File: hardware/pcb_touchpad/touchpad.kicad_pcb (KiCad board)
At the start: 2 copper layers, 41.3 x 30.3 mm, 24 parts, among them U1 IQS9151

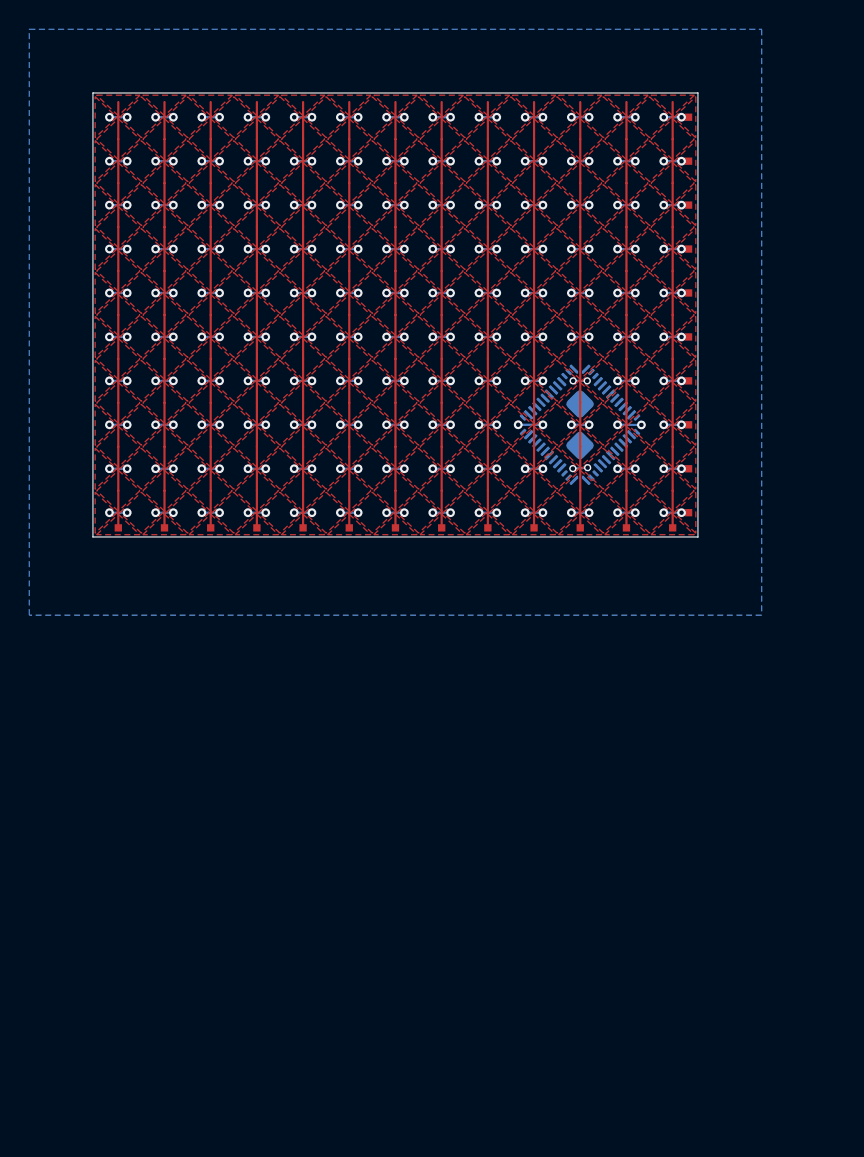
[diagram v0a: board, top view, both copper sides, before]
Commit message: touchpad: regenerated touchpad, made IQS7211E symbol
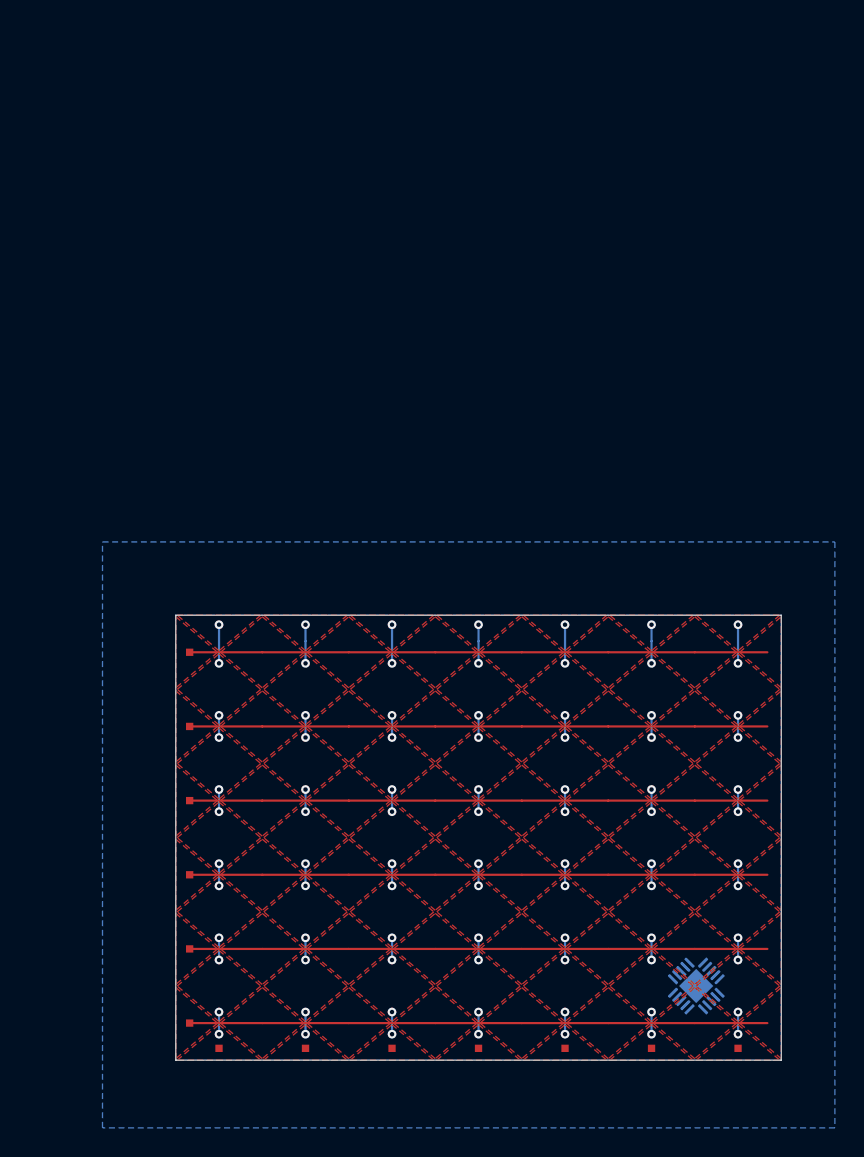
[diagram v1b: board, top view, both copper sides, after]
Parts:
- removed COL10, COL8, COL9, ROW10, ROW11, ROW12, ROW13, ROW7, ROW8, ROW9: TESTPOINTPAD_0_5MM, PAD_0_5MM
- U1: value IQS9151 -> IQS7211E; footprint Package_DFN_QFN:VQFN-52-1EP_6x6mm_P0.4mm_EP4.7x4.7mm -> Package_DFN_QFN:QFN-20-1EP_3x3mm_P0.4mm_EP1.65x1.65mm
- moved COL7 54.7 mm to (186.9, 134.6), turned to 0 degrees
- moved COL6 51.6 mm to (181.0, 134.6), turned to 0 degrees
- moved COL5 49.3 mm to (175.1, 134.6), turned to 0 degrees
- moved COL1 48.6 mm to (151.5, 134.6), turned to 0 degrees
- moved COL4 47.8 mm to (169.2, 134.6), turned to 0 degrees
- moved COL2 47.4 mm to (157.4, 134.6), turned to 0 degrees
- moved ROW1 47.2 mm to (149.5, 132.9), turned to 0 degrees
- moved COL3 47.1 mm to (163.3, 134.6), turned to 0 degrees
- moved ROW2 41.4 mm to (149.5, 127.8), turned to 0 degrees
- moved U1 39.1 mm to (184.0, 130.3), turned to 135 degrees
- moved ROW3 35.7 mm to (149.5, 122.7), turned to 0 degrees
- moved ROW4 30.0 mm to (149.5, 117.7), turned to 0 degrees
- moved ROW5 24.5 mm to (149.5, 112.6), turned to 0 degrees
- moved ROW6 19.2 mm to (149.5, 107.5), turned to 0 degrees
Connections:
- U1 pad 10: unconnected-(U1-NC-Pad10) -> /COL2
- U1 pad 11: /COL8 -> /COL1
- U1 pad 12: unconnected-(U1-NC-Pad12) -> /ROW6
- U1 pad 13: unconnected-(U1-NC-Pad13) -> /ROW5
- U1 pad 14: /COL7 -> /ROW4
- U1 pad 15: unconnected-(U1-NC-Pad15) -> /ROW3
- U1 pad 16: /COL6 -> /ROW2
- U1 pad 17: unconnected-(U1-NC-Pad17) -> /ROW1
- U1 pad 19: /COL5 -> unconnected-(U1-SDA-Pad19)
- U1 pad 21: /COL4 -> GND
- U1 pad 5: unconnected-(U1-VREG-Pad5) -> /COL7
- U1 pad 6: /COL10 -> /COL6
- U1 pad 7: unconnected-(U1-NC-Pad7) -> /COL5
- U1 pad 8: /COL9 -> /COL4
- U1 pad 9: unconnected-(U1-NC-Pad9) -> /COL3
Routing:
- net (no net): track 0.00 -> 71.4 mm, vias 0 -> 84
- net /ROW12: track 29.1 -> 0.00 mm
- net /ROW10: track 29.1 -> 0.00 mm
- net /ROW9: track 29.1 -> 0.00 mm
- net /ROW11: track 29.1 -> 0.00 mm
- net /ROW: track 29.1 -> 0.00 mm
- net /ROW8: track 29.1 -> 0.00 mm
- net /ROW13: track 29.1 -> 0.00 mm
- net /COL3: track 16.6 -> 0.00 mm, vias 26 -> 0
- net /COL9: track 15.8 -> 0.00 mm, vias 26 -> 0
- net /COL8: track 15.8 -> 0.00 mm, vias 26 -> 0
- net /COL7: track 15.8 -> 0.00 mm, vias 26 -> 0
- net /COL6: track 15.8 -> 0.00 mm, vias 26 -> 0
- net /COL5: track 15.8 -> 0.00 mm, vias 26 -> 0
- net /COL10: track 15.8 -> 0.00 mm, vias 26 -> 0
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- removed copper zone on F.Cu, net /COL10
- removed copper zone on F.Cu, net /COL8
- removed copper zone on F.Cu, net /COL9
- removed copper zone on F.Cu, net /ROW
- removed copper zone on F.Cu, net /ROW10
- removed copper zone on F.Cu, net /ROW11
- removed copper zone on F.Cu, net /ROW12
- removed copper zone on F.Cu, net /ROW13
- removed copper zone on F.Cu, net /ROW8
- removed copper zone on F.Cu, net /ROW9
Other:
- board size 41.3 x 30.3 mm -> 41.3 x 30.4 mm

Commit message: touchpad: changed nets for col vias, removed mask opening for test pads
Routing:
- net (no net): track 71.4 -> 0.00 mm, vias 84 -> 0
- net /COL7: track 0.00 -> 10.2 mm, vias 0 -> 12
- net /COL6: track 0.00 -> 10.2 mm, vias 0 -> 12
- net /COL5: track 0.00 -> 10.2 mm, vias 0 -> 12
- net /COL4: track 0.00 -> 10.2 mm, vias 0 -> 12
- net /COL3: track 0.00 -> 10.2 mm, vias 0 -> 12
- net /COL2: track 0.00 -> 10.2 mm, vias 0 -> 12
- net /COL1: track 0.00 -> 10.2 mm, vias 0 -> 12

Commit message: touchpad: moved stuff around
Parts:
- moved U1 23.7 mm to (160.3, 130.3)
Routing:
- net /COL7: track 10.2 -> 9.07 mm
- net /COL6: track 10.2 -> 9.07 mm
- net /COL5: track 10.2 -> 9.07 mm
- net /COL4: track 10.2 -> 9.07 mm
- net /COL3: track 10.2 -> 9.07 mm
- net /COL2: track 10.2 -> 9.07 mm
- net /COL1: track 10.2 -> 9.07 mm
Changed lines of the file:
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@@
 		(filling no)
 		(aux_axis_origin 148.5011 105.0036)
-		(grid_origin 148.5011 105.0036)
+		(grid_origin 154.4061 130.3186)
 		(pcbplotparams
 			(layerselection 0x00000000_00000000_55555555_5755f5ff)
@@
 	(footprint "Package_DFN_QFN:QFN-20-1EP_3x3mm_P0.4mm_EP1.65x1.65mm"
 		(layer "B.Cu")
-		(at 184.037545 130.3203 135)
+		(at 160.310065 130.3136 135)
 		(descr "QFN, 20 Pin (https://www.analog.com/media/en/technical-documentation/data-sheets/3553fc.pdf#page=34)")
 		(tags "QFN NoLead")
@@
 	)
 	(via
-		(at 151.453946 105.653612)
+		(at 151.453946 106.77924)
 		(size 0.6)
 		(drill 0.3)
@@
 	)
 	(segment
-		(start 151.453946 105.653612)
-		(end 151.453946 106.77924)
-		(width 0.15)
-		(layer "B.Cu")
-		(net "/COL1")
-	)
-	(segment
 		(start 151.45395 108.29134)
 		(end 151.45395 106.77924)
@@
 	)
 	(via
-		(at 169.1711 105.653612)
+		(at 169.1711 106.77924)
 		(size 0.6)
 		(drill 0.3)
@@
 	)
 	(segment
-		(start 169.1711 105.653612)
-		(end 169.1711 106.77924)
-		(width 0.15)
-		(layer "B.Cu")
-		(net "/COL4")
-	)
-	(segment
 		(start 169.1711 108.29134)
 		(end 169.1711 106.77924)
@@
 	)
 	(via
-		(at 175.0768 105.653612)
+		(at 175.0768 106.77924)
 		(size 0.6)
 		(drill 0.3)
@@
 	)
 	(segment
-		(start 175.0768 105.653612)
-		(end 175.0768 106.77924)
-		(width 0.15)
-		(layer "B.Cu")
-		(net "/COL5")
-	)
-	(segment
 		(start 175.0768 133.608)
 		(end 175.0768 132.0959)
@@
 	)
 	(via
-		(at 157.359633 105.653612)
+		(at 157.359633 106.77924)
 		(size 0.6)
 		(drill 0.3)
@@
 	)
 	(segment
-		(start 157.359633 105.653612)
-		(end 157.359633 106.77924)
-		(width 0.15)
-		(layer "B.Cu")
-		(net "/COL2")
-	)
-	(segment
 		(start 149.450034 122.725266)
 		(end 154.4068 122.725275)
@@
 	)
 	(via
-		(at 163.2654 105.653612)
+		(at 163.2654 106.77924)
 		(size 0.6)
 		(drill 0.3)
@@
 	)
 	(segment
-		(start 163.2654 105.653612)
-		(end 163.2654 106.77924)
-		(width 0.15)
-		(layer "B.Cu")
-		(net "/COL3")
-	)
-	(segment
 		(start 163.2654 113.35468)
 		(end 163.2654 111.84257)
@@
 	)
 	(via
-		(at 186.8882 105.653612)
+		(at 186.8882 106.77924)
 		(size 0.6)
 		(drill 0.3)
@@
 	)
 	(segment
-		(start 186.8882 105.653612)
-		(end 186.8882 106.77924)
-		(width 0.15)
-		(layer "B.Cu")
-		(net "/COL7")
-	)
-	(segment
 		(start 186.8882 128.5447)
 		(end 186.8882 127.0326)
@@
 	)
 	(via
-		(at 180.9825 105.653612)
+		(at 180.9825 106.77924)
 		(size 0.6)
 		(drill 0.3)
@@
 	)
 	(segment
-		(start 180.9825 105.653612)
-		(end 180.9825 106.77924)
-		(width 0.15)
-		(layer "B.Cu")
-		(net "/COL6")
-	)
-	(segment
 		(start 180.9825 133.608)
 		(end 180.9825 132.0959)
@@
 		(name "GND Fill")
 		(hatch edge 0.5)
-		(connect_pads
+		(connect_pads yes
 			(clearance 0.15)
 		)

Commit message: added conn to trackpad pcb, updated mockup, placed conn
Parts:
- added J1: 503480-0540, 5034800540:503480-0540, B.Cu at (151.5, 113.1)
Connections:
- U1 pad 18: unconnected-(U1-SCL-Pad18) -> Net-(U1-SCL)
- U1 pad 19: unconnected-(U1-SDA-Pad19) -> Net-(U1-SDA)
- U1 pad 20: unconnected-(U1-RDY/MCLR-Pad20) -> Net-(U1-RDY/MCLR)

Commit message: small stuff
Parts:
- added C1: 1u, Capacitor_SMD:C_0402_1005Metric, B.Cu at (155.9, 132.2)
- added C2: 1u, Capacitor_SMD:C_0402_1005Metric, B.Cu at (157.5, 131.3)
- added C3: 1u, Capacitor_SMD:C_0402_1005Metric, B.Cu at (157.7, 130.4)
- moved U1 5.99 mm to (154.4, 129.3)
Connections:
- J1 pad 4: +3V3 -> Net-(U1-RDY/MCLR)
- J1 pad 5: Net-(U1-RDY/MCLR) -> +3V3
- U1 pad 1: unconnected-(U1-VDD-Pad1) -> +3V3
- U1 pad 2: unconnected-(U1-VREGD-Pad2) -> Net-(U1-VREGD)
- U1 pad 4: unconnected-(U1-VREGA-Pad4) -> Net-(U1-VREGA)
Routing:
- net /ROW1: track 39.4 -> 81.6 mm, vias 0 -> 1
- net /COL7: track 9.07 -> 45.7 mm
- net /COL6: track 9.07 -> 40.4 mm
- net /COL2: track 9.07 -> 40.2 mm
- net /COL5: track 9.07 -> 35.4 mm
- net /ROW6: track 39.4 -> 63.9 mm, vias 0 -> 1
- net +3V3: track 0.00 -> 21.8 mm
- net Net-(U1-SCL): track 0.00 -> 21.5 mm
- net Net-(U1-SDA): track 0.00 -> 21.1 mm
- net /COL4: track 9.07 -> 30.1 mm
- net Net-(U1-RDY/MCLR): track 0.00 -> 20.8 mm
- net /ROW5: track 39.4 -> 57.5 mm, vias 0 -> 1
- net /COL3: track 9.07 -> 24.3 mm
- net /ROW4: track 39.4 -> 51.3 mm, vias 0 -> 1
- net /ROW3: track 39.4 -> 42.9 mm, vias 0 -> 1
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
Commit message: first touchpad draft
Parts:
- J1: footprint 5034800540:503480-0540 -> 503480-0540:503480-0540
- moved C3 5.32 mm to (154.3, 126.3), turned to 45 degrees
- moved C2 4.88 mm to (156.1, 126.7), turned to 45 degrees
- moved C1 3.58 mm to (157.8, 129.2), turned to 0 degrees
- turned U1 to -135 degrees
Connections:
- net Net-(U1-RDY/MCLR) renamed /RDY/MCLR
- net Net-(U1-SCL) renamed /SCL
- net Net-(U1-SDA) renamed /SDA
- net Net-(U1-VREGA) renamed /VREGA
- net Net-(U1-VREGD) renamed /VREGD
- J1 pad MP_1: (no net) -> GND
- J1 pad MP_2: (no net) -> GND
- U1 pad 12: /ROW6 -> /ROW1
- U1 pad 13: /ROW5 -> /ROW2
- U1 pad 14: /ROW4 -> /ROW3
- U1 pad 15: /ROW3 -> /ROW4
- U1 pad 16: /ROW2 -> /ROW5
- U1 pad 17: /ROW1 -> /ROW6
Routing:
- net /ROW1: track 81.6 -> 44.2 mm
- net /COL2: track 40.2 -> 11.8 mm
- net +3V3: track 21.8 -> 14.1 mm
- net /RDY/MCLR: track 20.8 -> 13.9 mm
- net /SDA: track 21.1 -> 14.3 mm
- net /SCL: track 21.5 -> 14.9 mm
- net /COL4: track 30.1 -> 23.6 mm
- net /COL3: track 24.3 -> 17.8 mm
- net /COL5: track 35.4 -> 29.3 mm
- net /ROW3: track 42.9 -> 48.8 mm
- net /COL6: track 40.4 -> 35.0 mm
- net /COL7: track 45.7 -> 41.3 mm
- net /ROW2: track 41.1 -> 44.7 mm
- net /ROW4: track 51.3 -> 54.1 mm
- net /COL1: track 10.3 -> 12.6 mm
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
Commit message: added lra to touchpad
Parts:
- added REF**: C10-100, LRA:C10-100, B.Cu at (169.2, 120.2)
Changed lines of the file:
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@@
 		(filling no)
 		(aux_axis_origin 148.5011 105.0036)
-		(grid_origin 154.4061 130.3186)
+		(grid_origin 169.1711 120.1936)
 		(pcbplotparams
 			(layerselection 0x00000000_00000000_55555555_5755f5ff)
@@
 			)
 		)
+	)
+	(footprint "LRA:C10-100"
+		(layer "B.Cu")
+		(at 169.1711 120.1936 180)
+		(property "Reference" "REF**"
+			(at 12.95 13.45 0)
+			(unlocked yes)
+			(layer "B.SilkS")
+			(hide yes)
+			(effects
+				(font
+					(size 1 1)
+					(thickness 0.1)
+				)
+				(justify mirror)
+			)
+		)
+		(property "Value" "C10-100"
+			(at 12.95 11.95 0)
+			(unlocked yes)
+			(layer "B.Fab")
+			(hide yes)
+			(effects
+				(font
+					(size 1 1)
+					(thickness 0.15)
+				)
+				(justify mirror)
+			)
+		)
+		(property "Datasheet" ""
+			(at 0 0 0)
+			(unlocked yes)
+			(layer "B.Fab")
+			(hide yes)
+			(effects
+				(font
+					(size 1 1)
+					(thickness 0.15)
+				)
+				(justify mirror)
+			)
+		)
+		(property "Description" ""
+			(at 0 0 0)
+			(unlocked yes)
+			(layer "B.Fab")
+			(hide yes)
+			(effects
+				(font
+					(size 1 1)
+					(thickness 0.15)
+				)
+				(justify mirror)
+			)
+		)
+		(attr smd)
+		(duplicate_pad_numbers_are_jumpers no)
+		(fp_line
+			(start 1.76 8.05)
+			(end 1.76 4.775)
+			(stroke
+				(width 0.1)
+				(type default)
+			)
+			(layer "B.SilkS")
+		)
+		(fp_line
+			(start -0.91 8.9)
+			(end 0.91 8.9)
+			(stroke
+				(width 0.1)
+				(type solid)
+			)
+			(layer "B.SilkS")
+		)
+		(fp_line
+			(start -1.76 8.05)
+			(end -1.76 4.8)
+			(stroke
+				(width 0.1)
+				(type default)
+			)
+			(layer "B.SilkS")
+		)
+		(fp_arc
+			(start 1.76 8.05)
+			(mid 1.511041 8.651041)
+			(end 0.91 8.9)
+			(stroke
+				(width 0.1)
+				(type default)
+			)
+			(layer "B.SilkS")
+		)
+		(fp_arc
+			(start -0.91 8.9)
+			(mid -1.511041 8.651041)
+			(end -1.76 8.05)
+			(stroke
+				(width 0.1)
+				(type default)
+			)
+			(layer "B.SilkS")
+		)
+		(fp_arc
+			(start -1.787619 4.764729)
+			(mid 0.014733 -5.089008)
+			(end 1.76 4.775)
+			(stroke
+				(width 0.1)
+				(type default)
+			)
+			(layer "B.SilkS")
+		)
+		(fp_text user "${REFERENCE}"
+			(at 14.6 14.575 0)
+			(unlocked yes)
+			(layer "B.Fab")
+			(effects
+				(font
+					(size 1 1)
+					(thickness 0.15)
+				)
+				(justify mirror)
+			)
+		)
+		(embedded_fonts no)
+		(model "/home/koeg/Repos/Projects/meko/hardware/pcb_lib/LRA/LRA.step"
+			(offset
+				(xyz 0 0 0.1)
+			)
+			(scale
+				(xyz 1 1 1)
+			)
+			(rotate
+				(xyz -0 -0 -90)
+			)
+		)

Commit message: added touchpad silkscreen
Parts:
- removed REF**: C10-100, LRA:C10-100
- added SYM1: Logo_Open_Hardware_Small, Symbol:OSHW-Logo2_14.6x12mm_SilkScreen, B.Cu at (182.0, 112.1)
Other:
- board text added: "V3.0.0"
- board text added: "gensis.xyz"
- board text added: "hey!"
